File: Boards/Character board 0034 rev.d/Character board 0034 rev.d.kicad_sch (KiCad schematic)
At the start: 40 parts, among them J1 card edge, J2 character connector, J3 power jumper, J4 return jumper, Q1 TIP130A, U1 2.2K, U1 6821, U13 7406, U2 2.2K, U4 ULN2003A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

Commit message: rev d layout done
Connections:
- net 24R: now also J4.3 (Pin_3); no longer C1.2, C25.1, J2.25 (Pin_25), J2.26 (Pin_26), J4.1 (Pin_1), J4.2 (Pin_2), U4.8 (GND), U4.8 (GND)
- net GND: now also J4.1 (Pin_1); no longer J4.3 (Pin_3)
- new net return out: C1.2, C25.1, J2.25 (Pin_25), J2.26 (Pin_26), J4.2 (Pin_2), U4.8 (GND), U4.8 (GND)
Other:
- moved on the sheet: CR1, J4
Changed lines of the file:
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@@
   (junction (at 205.105 119.38) (diameter 0) (color 0 0 0 0)
   )
-  (junction (at 173.355 114.3) (diameter 0) (color 0 0 0 0)
-  )
   (junction (at 82.55 96.52) (diameter 0) (color 0 0 0 0)
   )
@@
   )
   (junction (at 200.025 104.14) (diameter 0) (color 0 0 0 0)
+  )
+  (junction (at 34.925 20.32) (diameter 0) (color 0 0 0 0)
   )
   (junction (at 210.185 155.575) (diameter 0) (color 0 0 0 0)
@@
     (stroke (width 0) (type default))
   )
+  (wire (pts (xy 34.925 20.32) (xy 62.23 20.32))
+    (stroke (width 0) (type default))
+  )
   (wire (pts (xy 220.345 90.805) (xy 220.345 99.06))
     (stroke (width 0) (type default))
@@
     (stroke (width 0) (type default))
   )
-  (wire (pts (xy 51.435 20.32) (xy 62.23 20.32))
+  (wire (pts (xy 32.385 20.32) (xy 34.925 20.32))
     (stroke (width 0) (type default))
   )
@@
     (stroke (width 0) (type default))
   )
-  (wire (pts (xy 168.91 114.3) (xy 173.355 114.3))
-    (stroke (width 0) (type default))
-  )
   (wire (pts (xy 205.105 119.38) (xy 202.565 119.38))
     (stroke (width 0) (type default))
@@
     (stroke (width 0) (type default))
   )
-  (wire (pts (xy 227.33 113.03) (xy 186.055 113.03))
+  (wire (pts (xy 222.885 113.03) (xy 186.055 113.03))
     (stroke (width 0) (type default))
   )
@@
     )
   )
-  (global_label "GND" (shape input) (at 168.91 121.92 180) (fields_autoplaced)
-    (effects (font (size 1.27 1.27)) (justify right))
-    (property "Intersheetrefs" "${INTERSHEET_REFS}" (at 162.1337 121.92 0)
-      (effects (font (size 1.27 1.27)) (justify right) hide)
+  (global_label "GND" (shape input) (at 34.925 27.94 180) (fields_autoplaced)
+    (effects (font (size 1.27 1.27)) (justify right))
+    (property "Intersheetrefs" "${INTERSHEET_REFS}" (at 28.1487 27.94 0)
+      (effects (font (size 1.27 1.27)) (justify right) hide)
+    )
+  )
+  (global_label "return out" (shape input) (at 254.635 140.335 0) (fields_autoplaced)
+    (effects (font (size 1.27 1.27)) (justify left))
+    (property "Intersheetrefs" "${INTERSHEET_REFS}" (at 267.2168 140.335 0)
+      (effects (font (size 1.27 1.27)) (justify left) hide)
     )
   )
@@
     )
   )
-  (global_label "24R" (shape input) (at 227.33 113.03 0) (fields_autoplaced)
-    (effects (font (size 1.27 1.27)) (justify left))
-    (property "Intersheetrefs" "${INTERSHEET_REFS}" (at 233.9248 113.03 0)
+  (global_label "return out" (shape input) (at 222.885 113.03 0) (fields_autoplaced)
+    (effects (font (size 1.27 1.27)) (justify left))
+    (property "Intersheetrefs" "${INTERSHEET_REFS}" (at 235.4668 113.03 0)
       (effects (font (size 1.27 1.27)) (justify left) hide)
     )
@@
     )
   )
-  (global_label "24R" (shape input) (at 254.635 140.335 0) (fields_autoplaced)
-    (effects (font (size 1.27 1.27)) (justify left))
-    (property "Intersheetrefs" "${INTERSHEET_REFS}" (at 261.2298 140.335 0)
-      (effects (font (size 1.27 1.27)) (justify left) hide)
-    )
-  )
   (global_label "DBB1" (shape input) (at 40.005 96.52 0) (fields_autoplaced)
     (effects (font (size 1.27 1.27)) (justify left))
@@
     )
   )
+  (global_label "return out" (shape input) (at 241.935 140.335 180) (fields_autoplaced)
+    (effects (font (size 1.27 1.27)) (justify right))
+    (property "Intersheetrefs" "${INTERSHEET_REFS}" (at 229.3532 140.335 0)
+      (effects (font (size 1.27 1.27)) (justify right) hide)
+    )
+  )
   (global_label "BA1" (shape input) (at 22.225 109.22 180) (fields_autoplaced)
     (effects (font (size 1.27 1.27)) (justify right))
@@
     )
   )
-  (global_label "24R" (shape input) (at 241.935 140.335 180) (fields_autoplaced)
-    (effects (font (size 1.27 1.27)) (justify right))
-    (property "Intersheetrefs" "${INTERSHEET_REFS}" (at 235.3402 140.335 0)
-      (effects (font (size 1.27 1.27)) (justify right) hide)
-    )
-  )
   (global_label "A6out" (shape input) (at 254.635 125.095 0) (fields_autoplaced)
     (effects (font (size 1.27 1.27)) (justify left))
@@
     )
   )
-  (global_label "24R" (shape input) (at 51.435 20.32 180) (fields_autoplaced)
-    (effects (font (size 1.27 1.27)) (justify right))
-    (property "Intersheetrefs" "${INTERSHEET_REFS}" (at 44.8402 20.32 0)
+  (global_label "24R" (shape input) (at 32.385 20.32 180) (fields_autoplaced)
+    (effects (font (size 1.27 1.27)) (justify right))
+    (property "Intersheetrefs" "${INTERSHEET_REFS}" (at 25.7902 20.32 0)
       (effects (font (size 1.27 1.27)) (justify right) hide)
     )
@@
     )
   )
-  (symbol (lib_id "Connector_Generic:Conn_01x03") (at 64.77 13.97 90) (unit 1)
-    (in_bom yes) (on_board yes) (dnp no) (fields_autoplaced)
-    (property "Reference" "J4" (at 69.342 13.3263 90)
+  (symbol (lib_id "Connector_Generic:Conn_01x03") (at 64.77 13.97 270) (mirror x) (unit 1)
+    (in_bom yes) (on_board yes) (dnp no)
+    (property "Reference" "J4" (at 60.198 13.3263 90)
       (effects (font (size 1.27 1.27)) (justify right))
     )
-    (property "Value" "return jumper" (at 69.342 15.2473 90)
+    (property "Value" "return jumper" (at 60.198 15.2473 90)
       (effects (font (size 1.27 1.27)) (justify right))
     )
@@
     )
   )
-  (symbol (lib_id "Diode:1N4001") (at 168.91 118.11 90) (unit 1)
+  (symbol (lib_id "Diode:1N4001") (at 34.925 24.13 90) (unit 1)
     (in_bom yes) (on_board yes) (dnp no) (fields_autoplaced)
-    (property "Reference" "CR1" (at 170.942 117.4663 90)
+    (property "Reference" "CR1" (at 36.957 23.4863 90)
       (effects (font (size 1.27 1.27)) (justify right))
     )
-    (property "Value" "1N4001" (at 170.942 119.3873 90)
+    (property "Value" "1N4001" (at 36.957 25.4073 90)
       (effects (font (size 1.27 1.27)) (justify right))
     )
-    (property "Footprint" "Diode_THT:D_DO-41_SOD81_P12.70mm_Horizontal" (at 168.91 118.11 0)
-      (effects (font (size 1.27 1.27)) hide)
-    )
-    (property "Datasheet" "http://www.vishay.com/docs/88503/1n4001.pdf" (at 168.91 118.11 0)
-      (effects (font (size 1.27 1.27)) hide)
-    )
-    (property "Sim.Device" "D" (at 168.91 118.11 0)
-      (effects (font (size 1.27 1.27)) hide)
-    )
-    (property "Sim.Pins" "1=K 2=A" (at 168.91 118.11 0)
-      (effects (font (size 1.27 1.27)) hide)
-    )
+    (property "Footprint" "Diode_THT:D_DO-41_SOD81_P12.70mm_Horizontal" (at 34.925 24.13 0)
+      (effects (font (size 1.27 1.27)) hide)
+    )
+    (property "Datasheet" "http://www.vishay.com/docs/88503/1n4001.pdf" (at 34.925 24.13 0)
+      (effects (font (size 1.27 1.27)) hide)
+    )
+    (property "Sim.Device" "D" (at 34.925 24.13 0)
+      (effects (font (size 1.27 1.27)) hide)
+    )
+    (property "Sim.Pins" "1=K 2=A" (at 34.925 24.13 0)
+      (effects (font (size 1.27 1.27)) hide)
+    )

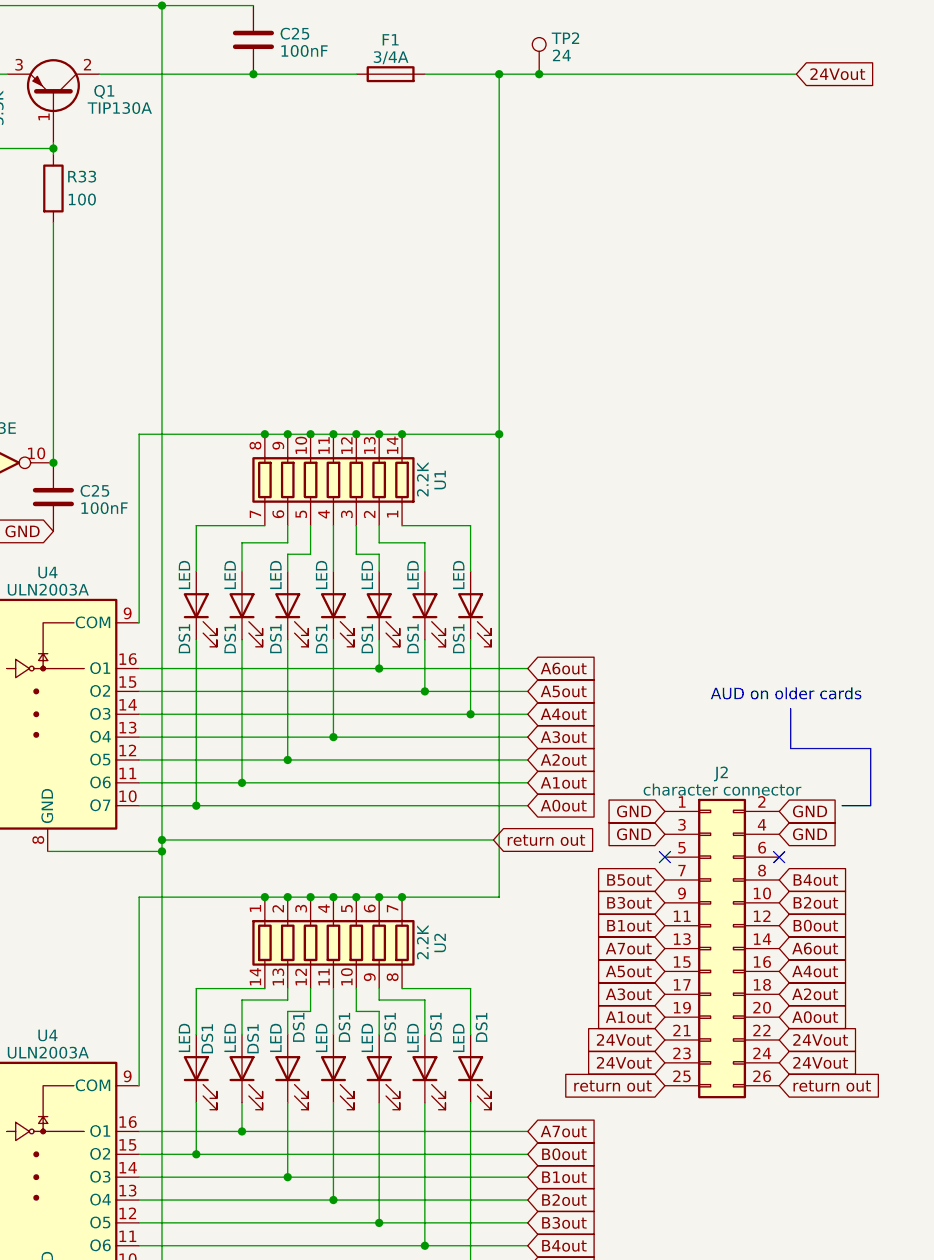
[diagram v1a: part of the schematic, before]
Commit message: finish light board rev.a, rename files, add renders and schematics, move pictures
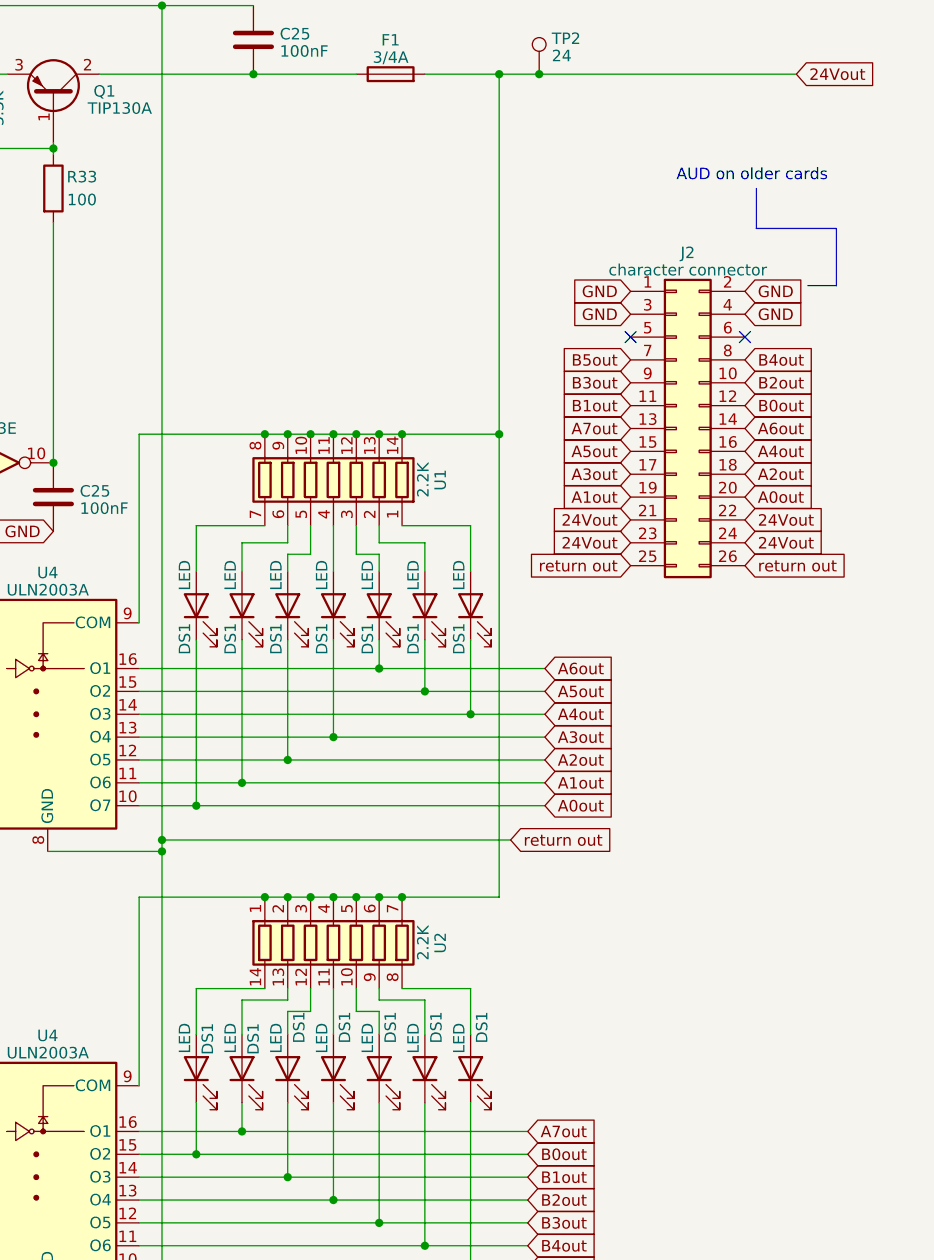
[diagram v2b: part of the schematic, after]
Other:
- moved on the sheet: J2

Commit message: revisions from real life boards
tip130a is actually tip30a, widened holes for crystal, widened holes for big power resistor, fixed cpu board LED resistors
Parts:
- Q1: value TIP130A -> TIP30A
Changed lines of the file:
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@@
       (effects (font (size 1.27 1.27)) (justify left))
     )
-    (property "Value" "TIP130A" (at 177.8 31.75 90)
+    (property "Value" "TIP30A" (at 177.8 31.75 90)
       (effects (font (size 1.27 1.27)) (justify left))
     )

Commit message: revised value of resistor to 1k per board
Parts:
- R33: value 100 -> 1K
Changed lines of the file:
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@@
       (effects (font (size 1.27 1.27)))
     )
-    (property "Value" "100" (at 177.165 41.91 0)
+    (property "Value" "1K" (at 177.165 41.91 0)
       (effects (font (size 1.27 1.27)))
     )
